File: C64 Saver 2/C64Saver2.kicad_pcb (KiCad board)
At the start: 2 copper layers, 43.9 x 28.8 mm, 21 parts, among them J1 Conn_01x04, J2 Conn_01x08, J4 Conn_01x08, J5 Conn_01x04, J6 Conn_01x04, Q1 2N7002, Q2 Q_PMOS_GDS

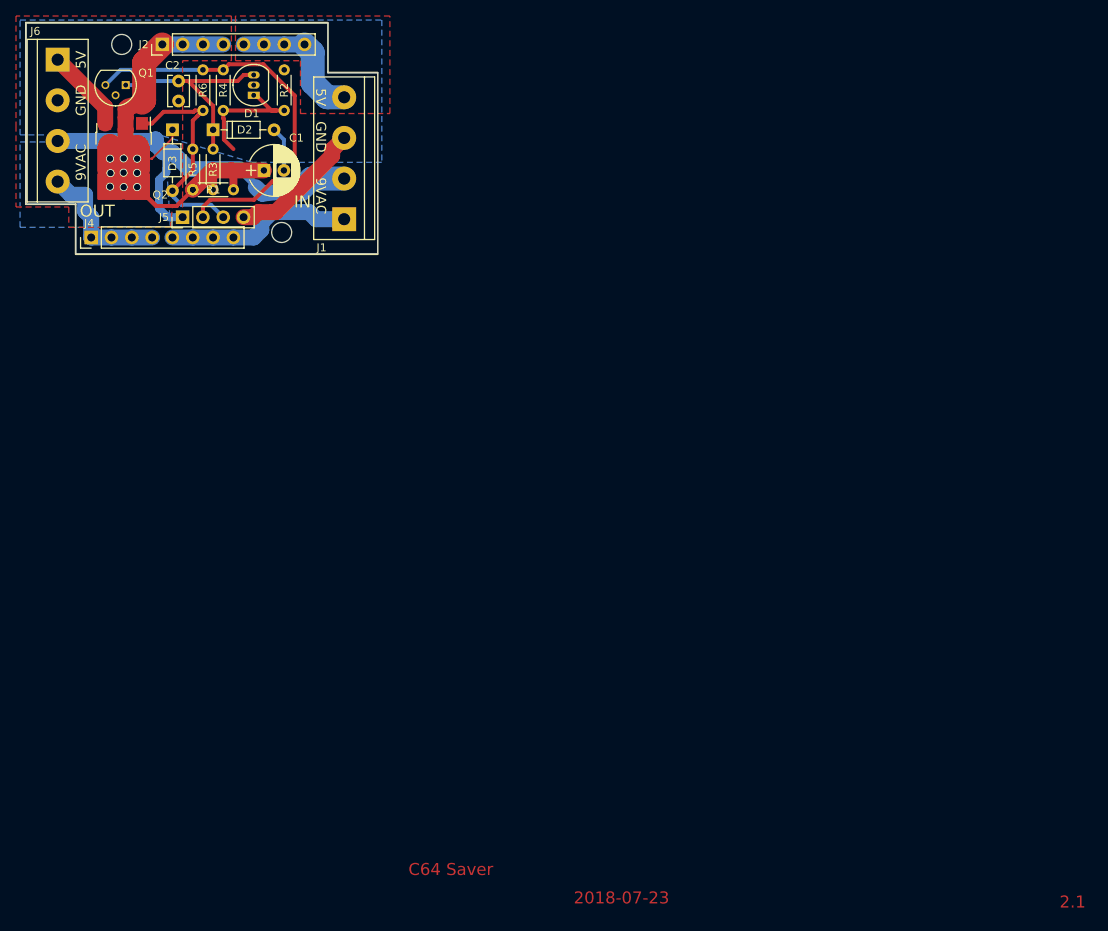
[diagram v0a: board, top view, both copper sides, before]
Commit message: Editting V2.2. R1 was rotated. why.
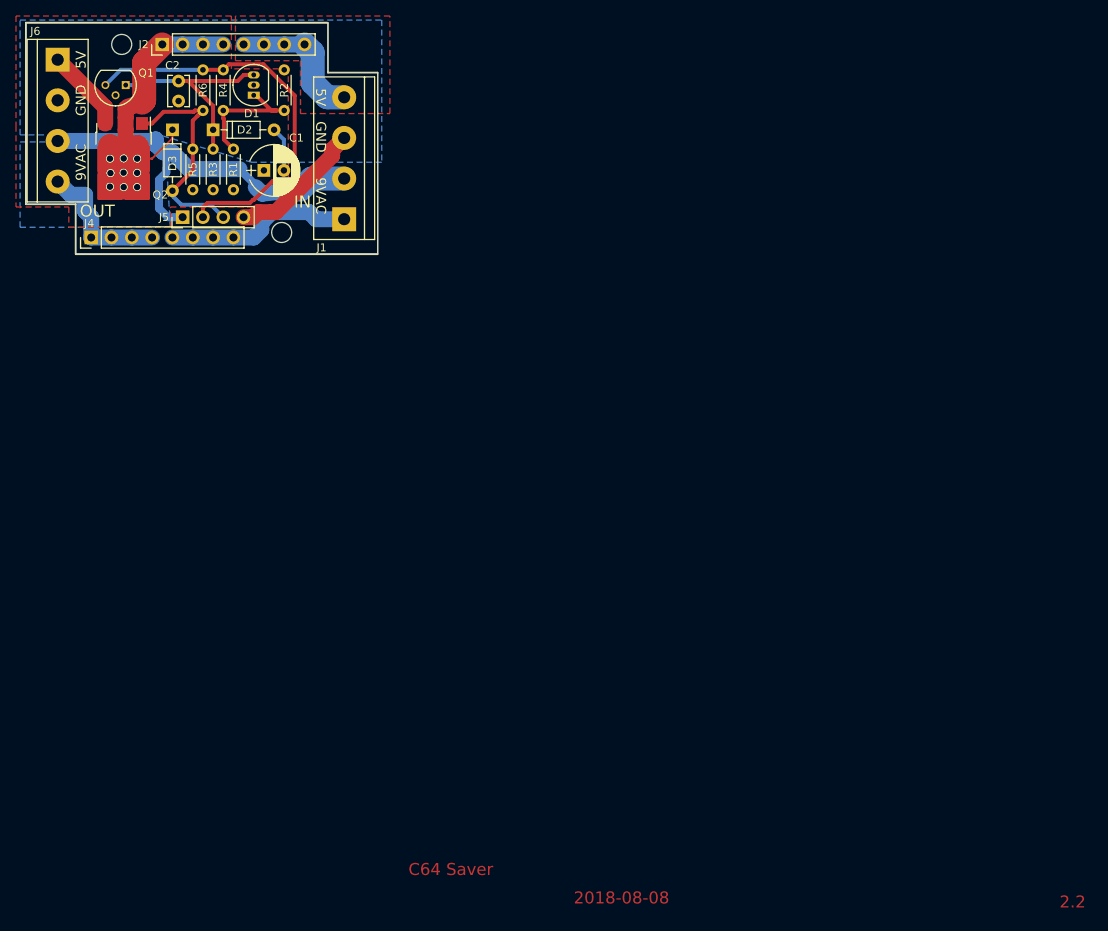
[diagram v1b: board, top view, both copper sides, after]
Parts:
- turned R1 to 90 degrees
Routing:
- net /VCC1-: track 88.1 -> 65.3 mm
- net /SENSE: track 22.9 -> 16.6 mm
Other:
- board text added: "2.2"
- board text added: "2018-08-08"
- board text added: "C64 Saver Rev 2.2 BWACK 2018"
- board text removed: "2.1"
- board text removed: "2018-07-23"
- board text removed: "C64 Saver Rev 2.1 BWACK 2018"

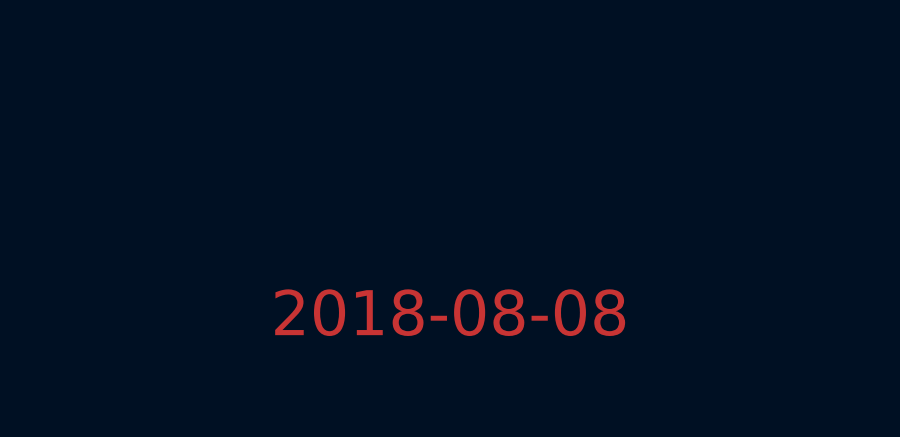
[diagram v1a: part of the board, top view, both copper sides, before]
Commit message: release saver v2.2
got fix for rotated resistor
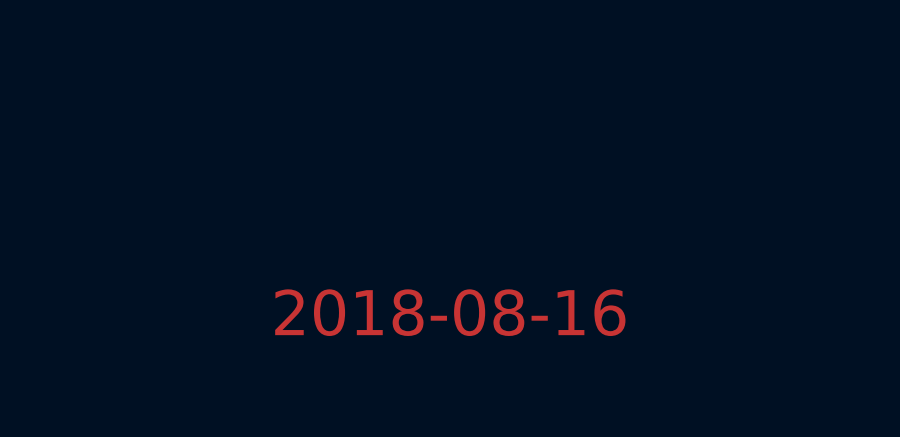
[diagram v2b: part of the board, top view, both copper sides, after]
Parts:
- R1, R6: value R -> 3k9
- R2, R3: value R -> 3k3
- R4: value R -> 330k
- R5: value R -> 33k
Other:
- board text added: "2018-08-16"
- board text removed: "2018-08-08"
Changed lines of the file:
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@@
     (links 50)
     (no_connects 0)
-    (area 138.051429 81.475 273.057714 194.898)
+    (area 140.386999 83.617999 184.479001 112.597001)
     (thickness 1.6)
     (drawings 26)
@@
       (effects (font (size 1 1) (thickness 0.15)))
     )
-    (fp_text value R (at 2.54 1.86 90) (layer F.Fab)
+    (fp_text value 3k9 (at 2.54 1.86 90) (layer F.Fab)
       (effects (font (size 1 1) (thickness 0.15)))
     )
@@
       (effects (font (size 1 1) (thickness 0.15)))
     )
-    (fp_text value R (at 2.54 1.86 90) (layer F.Fab)
+    (fp_text value 3k3 (at 2.54 1.86 90) (layer F.Fab)
       (effects (font (size 1 1) (thickness 0.15)))
     )
@@
       (effects (font (size 1 1) (thickness 0.15)))
     )
-    (fp_text value R (at 2.54 1.86 90) (layer F.Fab)
+    (fp_text value 3k3 (at 2.54 1.86 90) (layer F.Fab)
       (effects (font (size 1 1) (thickness 0.15)))
     )
@@
       (effects (font (size 1 1) (thickness 0.15)))
     )
-    (fp_text value R (at 2.54 1.86 90) (layer F.Fab)
+    (fp_text value 330k (at 2.54 1.86 90) (layer F.Fab)
       (effects (font (size 1 1) (thickness 0.15)))
     )
@@
       (effects (font (size 1 1) (thickness 0.15)))
     )
-    (fp_text value R (at 2.54 1.86 90) (layer F.Fab)
+    (fp_text value 33k (at 2.54 1.86 90) (layer F.Fab)
       (effects (font (size 1 1) (thickness 0.15)))
     )
@@
       (effects (font (size 1 1) (thickness 0.15)))
     )
-    (fp_text value R (at 2.54 1.86 90) (layer F.Fab)
+    (fp_text value 3k9 (at 2.54 1.86 90) (layer F.Fab)
       (effects (font (size 1 1) (thickness 0.15)))
     )
@@
     )
   )
-  (gr_text 2018-08-08 (at 214.884 193.04) (layer F.Cu)
+  (gr_text 2018-08-16 (at 214.884 193.04) (layer F.Cu)
     (effects (font (size 1.5 1.5) (thickness 0.3)))
   )

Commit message: v2.3
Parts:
- Q1: value 2N7002 -> 2N7000
- Q2: value Q_PMOS_GDS -> IRFR5305
- R5: value 33k -> 3k3
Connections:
- Q1 pad 1: /NGATE -> GND
- Q1 pad 2: GND -> /NGATE
- Q2 pad 2: /VCC1- -> /5V_SAFE
- Q2 pad 3: /5V_SAFE -> /VCC1-
- R5 pad 2: PGATE -> OVERVOLTAGE
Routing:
- net /VCC1-: track 65.3 -> 48.7 mm, vias 9 -> 0
- net /5V_SAFE: track 10.4 -> 23.0 mm, vias 0 -> 9
- net OVERVOLTAGE: track 50.7 -> 56.4 mm
- net /NGATE: track 26.4 -> 29.8 mm
- net PGATE: track 29.3 -> 32.2 mm
- added copper zone on B.Cu, net /5V_SAFE
- added copper zone on F.Cu, net /5V_SAFE
- removed copper zone on B.Cu, net /VCC1-
- removed copper zone on F.Cu, net /VCC1-
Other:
- board text added: "2.3"
- board text added: "2018-08-18"
- board text added: "C64 Saver Rev 2.3 BWACK 2018"
- board text removed: "2.2"
- board text removed: "2018-08-16"
- board text removed: "C64 Saver Rev 2.2 BWACK 2018"

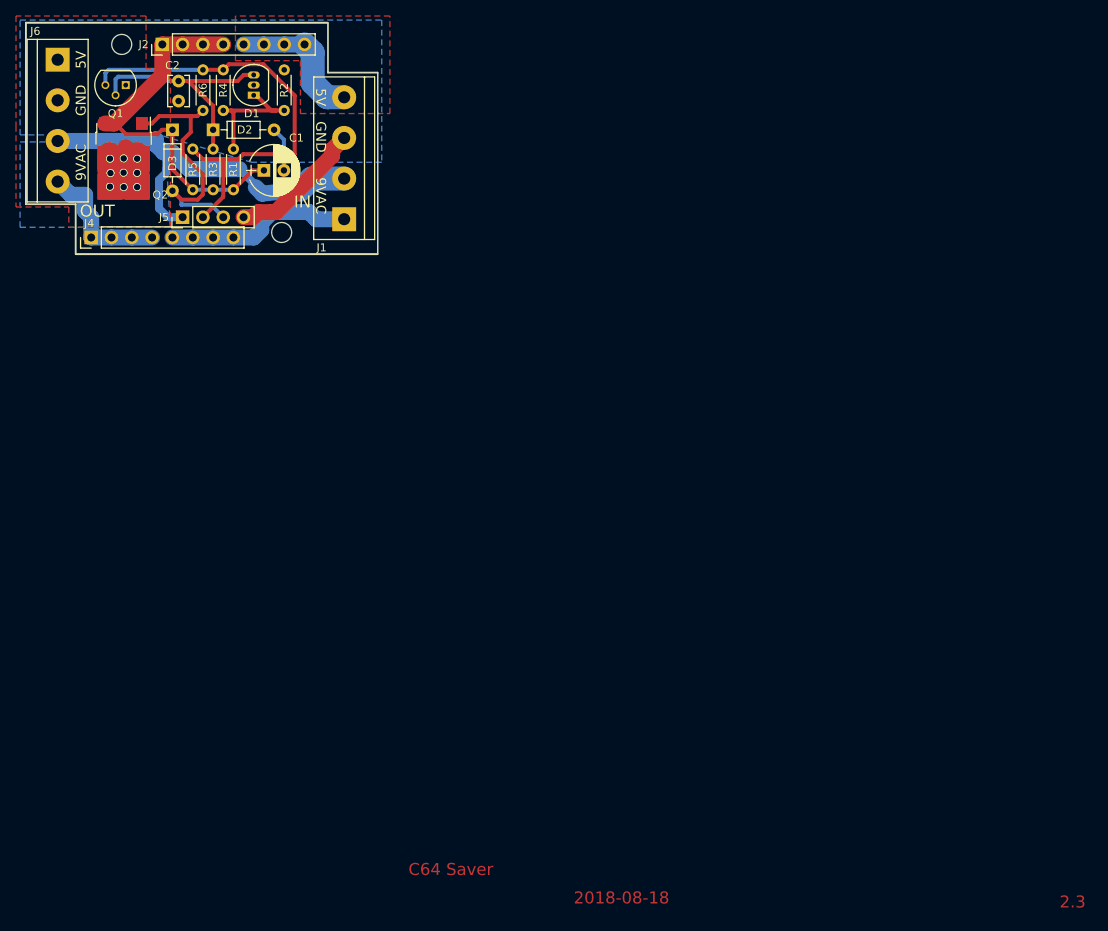
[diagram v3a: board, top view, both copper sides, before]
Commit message: New layout new routing. Resistor divider to support low Vth. #13
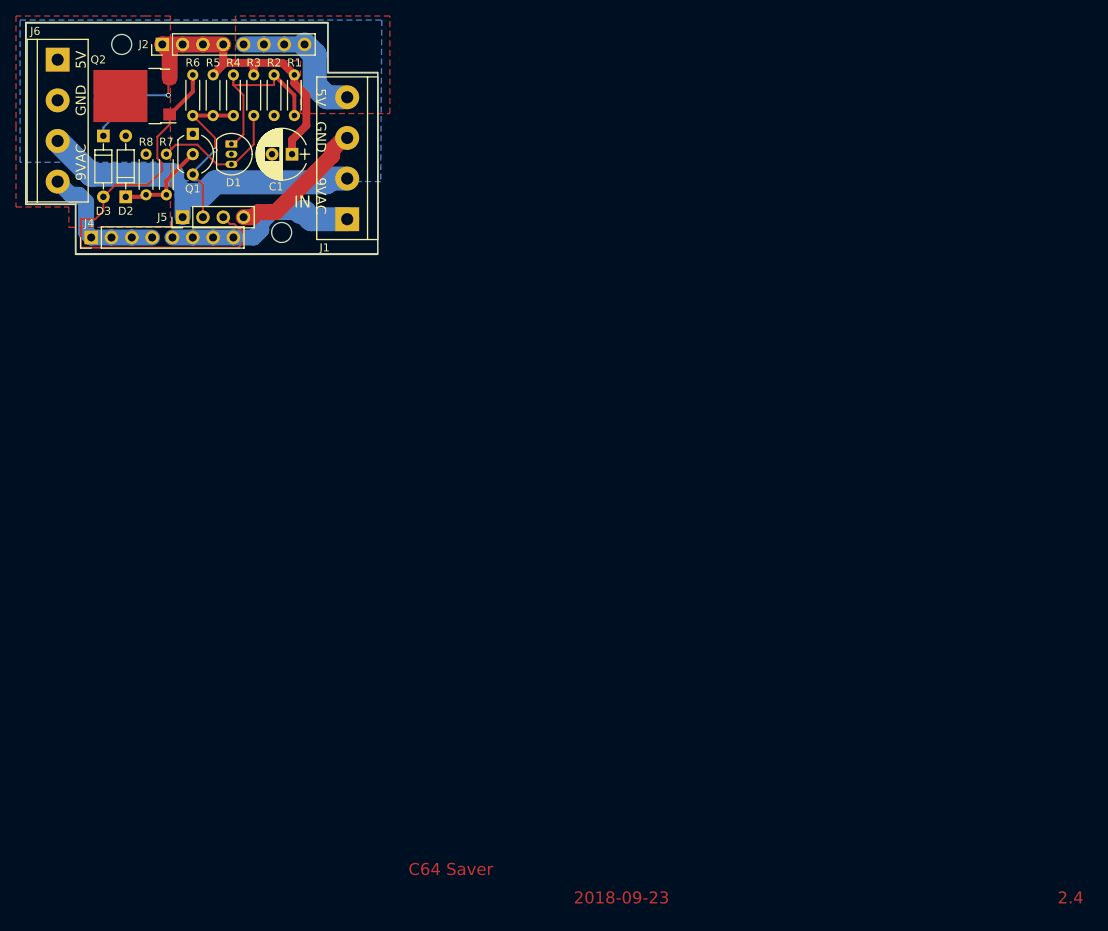
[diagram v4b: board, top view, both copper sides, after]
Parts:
- removed C2: 0.1uF, Capacitors_THT:C_Disc_D3.8mm_W2.6mm_P2.50mm
- added R7: 33k, Resistors_THT:R_Axial_DIN0204_L3.6mm_D1.6mm_P5.08mm_Horizontal, F.Cu at (158.0, 100.1)
- added R8: 82k, Resistors_THT:R_Axial_DIN0204_L3.6mm_D1.6mm_P5.08mm_Horizontal, F.Cu at (155.4, 105.2)
- Q1: footprint TO_SOT_Packages_THT:TO-92_Molded_Narrow -> TO_SOT_Packages_THT:TO-92_Inline_Wide
- moved R1 16.2 mm to (174.0, 90.2), turned to 270 degrees
- moved R3 15.2 mm to (168.9, 90.2), turned to 270 degrees
- moved R5 14.6 mm to (163.8, 90.2), turned to 270 degrees
- moved D2 13.8 mm to (152.9, 105.4), turned to 90 degrees
- moved Q1 10.4 mm to (161.3, 97.5), turned to 270 degrees
- moved D3 8.67 mm to (150.1, 97.8)
- moved Q2 7.90 mm to (154.0, 92.8), turned to 180 degrees
- moved D1 6.71 mm to (166.1, 98.8), turned to 270 degrees
- moved R2 4.62 mm to (171.4, 90.2), turned to 270 degrees
- moved R4 4.62 mm to (166.4, 90.2), turned to 270 degrees
- moved R6 4.62 mm to (161.3, 90.2), turned to 270 degrees
- moved C1 4.06 mm to (173.7, 100.1), turned to 180 degrees
- moved J1 0.38 mm to (180.6, 108.2)
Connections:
- D1 pad 3: /NGATE -> Net-(D1-Pad3)
- R3 pad 2: /NGATE -> Net-(D1-Pad3)
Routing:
- net OVERVOLTAGE: track 56.4 -> 21.3 mm, vias 0 -> 1
- net PGATE: track 32.2 -> 56.4 mm
- net /5V_SAFE: track 23.0 -> 0.00 mm, vias 9 -> 0
- net /NGATE: track 29.8 -> 11.6 mm
- net Net-(D1-Pad3): track 0.00 -> 17.1 mm
- net /9VAC2: track 51.2 -> 44.1 mm
- net /SENSE: track 16.2 -> 22.4 mm
- net /9VAC1: track 23.7 -> 29.9 mm
- net GND: track 22.7 -> 17.1 mm
- net /VCC1-: track 48.7 -> 51.9 mm, vias 0 -> 1
- removed copper zone on B.Cu, net /5V_SAFE
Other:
- board text added: "2.4"
- board text added: "2018-09-23"
- board text added: "C64 Saver Rev 2.4 BWACK 2018"
- board text removed: "2.3"
- board text removed: "2018-08-18"
- board text removed: "C64 Saver Rev 2.3 BWACK 2018"
- board text removed: "OUT"
